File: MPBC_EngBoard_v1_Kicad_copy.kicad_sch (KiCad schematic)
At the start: 4 parts, among them Q1 NMOS, Q2 NMOS, U2 MP1909

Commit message: Gate Driver Circuit Progress (commit test)
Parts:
- added C1: 4.7uF, symbol Device:C
- added C2: 1uF, symbol Device:C
- added C3: 10uF, symbol Device:C
- added D1, D2, D3: MBR053T1G, symbol Device:D_Schottky
- added R2: 1.6Ω, symbol Device:R_US
- added R3: 4.7Ω, symbol Device:R_US
- R1: value R_US -> 1.6Ω
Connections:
- net at Q1.2 (G): now also R1.1, D1.2 (A)
- net at Q1.3 (S), Q2.1 (D): now also U2.6 (SW), C1.2
- net at R1.2: now also U2.5 (DRVH), D1.1 (K)
- net at Q2.2 (G): now also D2.2 (A), R2.1
- net at U2.1 (BST): now also D3.1 (K), R3.2
- net VCC: now reaches U2.4 (VCC)
- net VCC: now also C2.1, C3.1, D3.2 (A)
- net GND: now reaches U2.7 (GND)
- net GND: now also C2.2, C3.2
- net at U2.8 (DRVL): now also D2.1 (K), R2.2
- new net: C1.1, R3.1
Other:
- title: (none) -> Buck Converter Channel
- moved on the sheet: Q1, R1, U2

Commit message: Started LDO
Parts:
- added C4, C6, C7: 10uF, symbol Device:C
- added C5: 1uF, symbol Device:C
- added R4: 133Ω, symbol Device:R_US
- added R5: 400Ω, symbol Device:R_US
- added U1: LM1084-ADJ, symbol Regulator_Linear:LM1084-ADJ
- Q1, Q2: value NMOS -> BSZ018N04LS6
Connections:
- net GND: now also Q2.3 (S), C6.2, C7.2, R5.2
- net VCC renamed VREG
- net VREG: now also C6.1, C7.1, R4.1, U1.2 (VO)
- new net: R4.2, R5.1, U1.1 (ADJ)

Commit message: Buck Converter Circuit Finished
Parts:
- added C10, C9: 2.2nF, symbol Device:C
- added C11, C12, C13: 100uF, symbol Device:C_Polarized_US
- added C14, C15, C16, C17, C18, C19, C20, C21: 22uF, symbol Device:C
- added C8: 22nF, 0603, symbol Device:C
- added L1: 7.6uH, symbol Device:L
- added R10: 500uΩ, symbol Device:R_US
- added R6, R7: 0Ω, symbol Device:R_US
- added R8, R9: 750mΩ, symbol Device:R_US
- R4: value 133Ω -> 130Ω
- R5: value 400Ω -> 910Ω
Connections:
- net GND: now also C4.2, C5.2, C10.2, C11.2, C12.2, C13.2, C14.2, C15.2, C16.2, C17.2, C18.2, C19.2, C20.2, C21.2, C8.2, R6.2, R7.2; no longer C6.2, C7.2
- net BUCK_SW: now reaches C1.2, Q1.3 (S), Q2.1 (D), U2.6 (SW)
- net BUCK_SW: now also C9.2, L1.1, R9.1
- net VCC: now reaches C5.1
- net VCC: now also C4.1, U1.3 (VI)
- net VDD: now reaches Q1.1 (D)
- net VDD: now also R8.1
- net H_GATE: now reaches D1.2 (A), Q1.2 (G), R1.1
- net LDO_FB: now reaches R4.2, R5.1, U1.1 (ADJ)
- net LDO_FB: now also C8.1
- net GD_DRVH: now reaches D1.1 (K), R1.2, U2.5 (DRVH)
- net GD_DRVL: now reaches D2.1 (K), R2.2, U2.8 (DRVL)
- net L_GATE: now reaches D2.2 (A), Q2.2 (G), R2.1
- net GD_BST: now reaches D3.1 (K), R3.2, U2.1 (BST)
- new net: C9.1, R8.2
- new net: C10.1, R9.2
- new net: C6.2, R6.1
- new net: C7.2, R7.1
- new net BUCK_OUT: C11.1, C12.1, C13.1, C14.1, C15.1, C16.1, C17.1, C18.1, C19.1, C20.1, C21.1, L1.2, R10.1
- new net V_OUT: R10.2
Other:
- moved on the sheet: C1, C2, C3, C4, C5, C6, C7, D1, D2, D3, Q1, Q2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

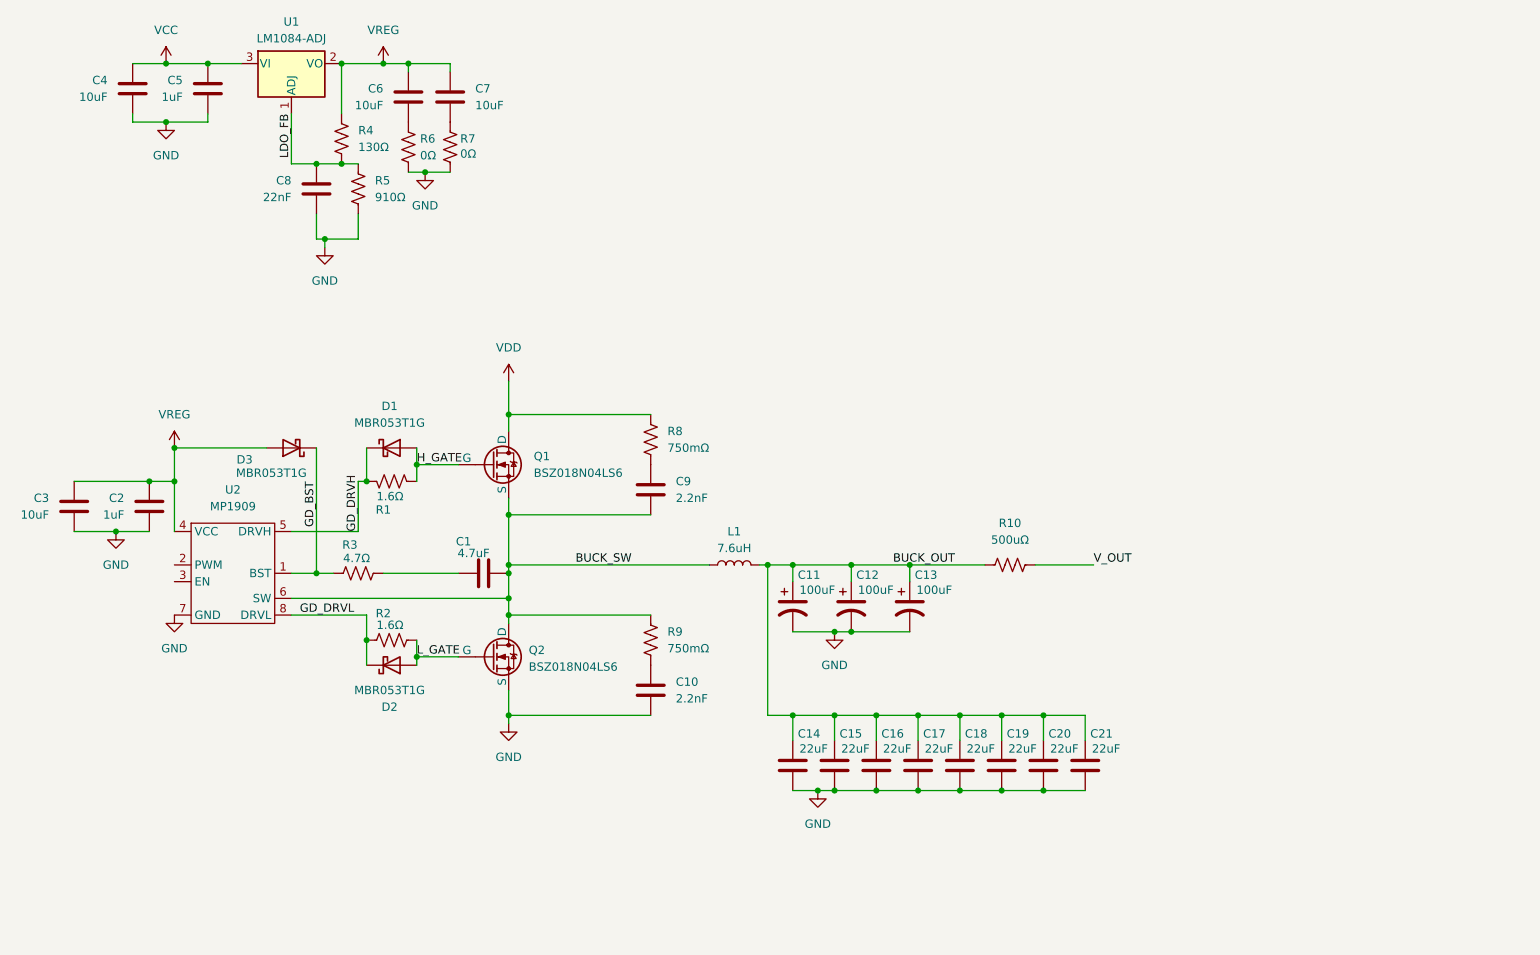
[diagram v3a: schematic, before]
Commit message: Updated to TPS7A24 regulator
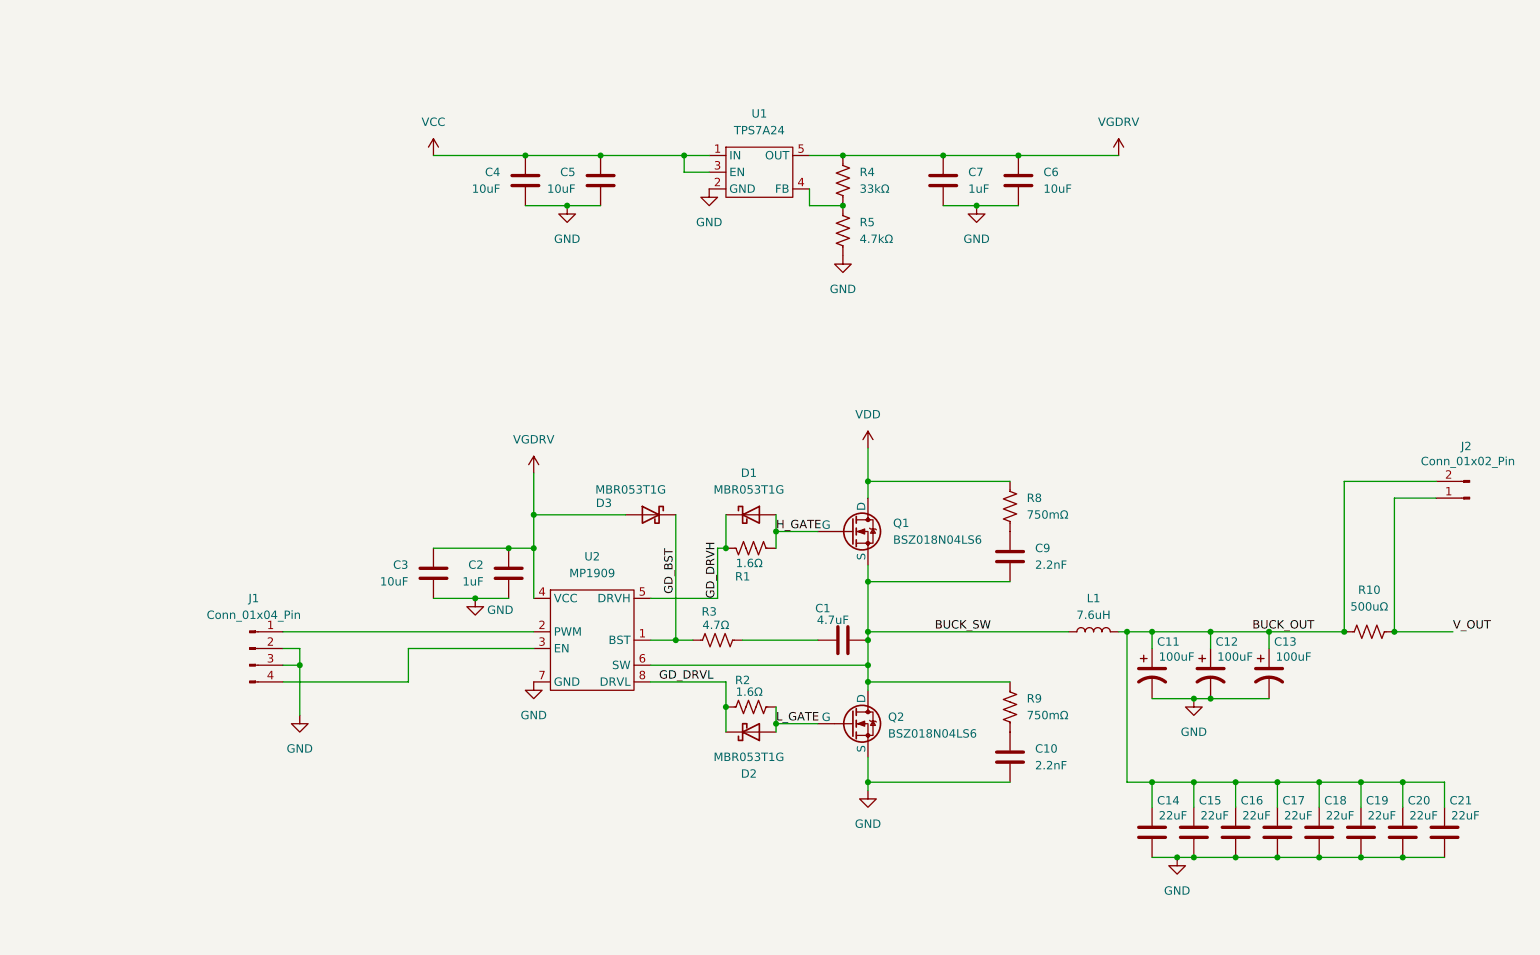
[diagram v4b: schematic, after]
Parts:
- removed C8: 22nF, 0603, symbol Device:C
- removed R6, R7: 0Ω, symbol Device:R_US
- removed U1: LM1084-ADJ, symbol Regulator_Linear:LM1084-ADJ
- added J1: Conn_01x04_Pin, symbol Connector:Conn_01x04_Pin
- added J2: Conn_01x02_Pin, symbol Connector:Conn_01x02_Pin
- added U1: TPS7A24, symbol MPBC_SchLib:TPS7A24
- C5: value 1uF -> 10uF
- C7: value 10uF -> 1uF
- R4: value 130Ω -> 33kΩ
- R5: value 910Ω -> 4.7kΩ
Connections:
- net BUCK_OUT: now also J2.2 (Pin_2)
- net GND: now also C6.2, C7.2, J1.2 (Pin_2), J1.3 (Pin_3), U1.2 (GND)
- net VCC: now also U1.1 (IN), U1.3 (EN)
- net V_OUT: now also J2.1 (Pin_1)
- net at U2.2 (PWM): now also J1.1 (Pin_1)
- net at U2.3 (EN): now also J1.4 (Pin_4)
- net LDO_FB: no longer names the net of R4.2, R5.1
- net LDO_FB: now also U1.4 (FB)
- net VREG renamed VGDRV
- net VGDRV: now also U1.5 (OUT)
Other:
- title: Buck Converter Channel -> Buck Converter Single Phase
- moved on the sheet: C1, C10, C11, C12, C13, C14, C15, C16, C17, C18, C19, C2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

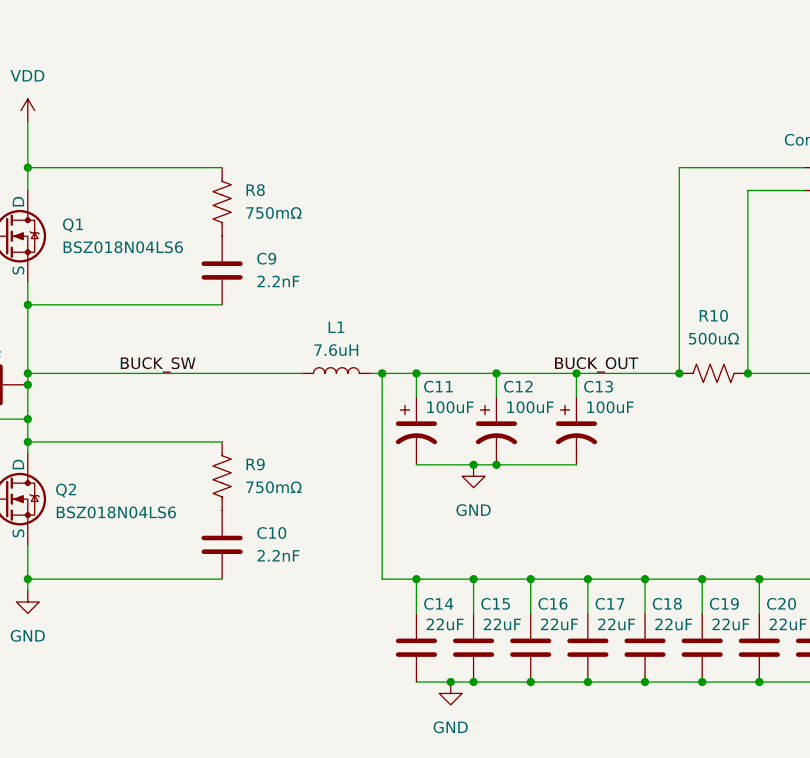
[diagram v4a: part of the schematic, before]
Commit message: DNP for snubber and most output caps
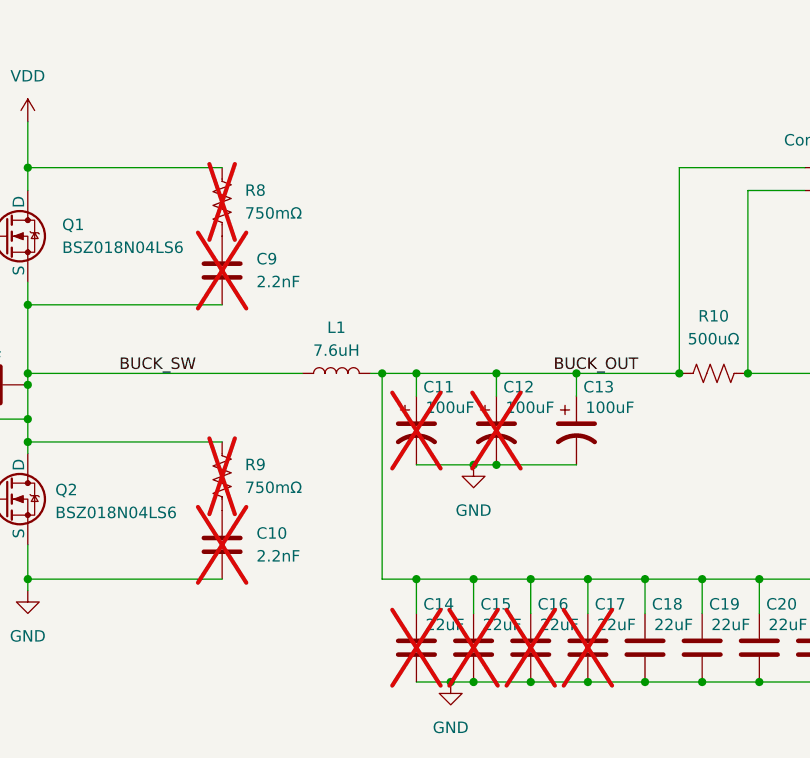
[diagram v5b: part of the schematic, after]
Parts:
- C10, C11, C12, C14, C15, C16, C17, C9, R8, R9: now not fitted
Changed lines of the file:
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@@
 		(in_bom yes)
 		(on_board yes)
-		(dnp no)
+		(dnp yes)
 		(fields_autoplaced yes)
 		(property "Reference" "R8"
@@
 		(in_bom yes)
 		(on_board yes)
-		(dnp no)
+		(dnp yes)
 		(property "Reference" "C9"
 			(at 166.37 97.7899 0)
@@
 		(in_bom yes)
 		(on_board yes)
-		(dnp no)
+		(dnp yes)
 		(property "Reference" "C12"
 			(at 193.802 112.014 0)
@@
 		(in_bom yes)
 		(on_board yes)
-		(dnp no)
+		(dnp yes)
 		(property "Reference" "C14"
 			(at 184.912 136.144 0)
@@
 		(in_bom yes)
 		(on_board yes)
-		(dnp no)
+		(dnp yes)
 		(property "Reference" "C11"
 			(at 184.912 112.014 0)
@@
 		(in_bom yes)
 		(on_board yes)
-		(dnp no)
+		(dnp yes)
 		(fields_autoplaced yes)
 		(property "Reference" "R9"
@@
 		(in_bom yes)
 		(on_board yes)
-		(dnp no)
+		(dnp yes)
 		(property "Reference" "C16"
 			(at 197.612 136.144 0)
@@
 		(in_bom yes)
 		(on_board yes)
-		(dnp no)
+		(dnp yes)
 		(property "Reference" "C15"
 			(at 191.262 136.144 0)
@@
 		(in_bom yes)
 		(on_board yes)
-		(dnp no)
+		(dnp yes)
 		(property "Reference" "C10"
 			(at 166.37 128.2699 0)
@@
 		(in_bom yes)
 		(on_board yes)
-		(dnp no)
+		(dnp yes)
 		(property "Reference" "C17"
 			(at 203.962 136.144 0)

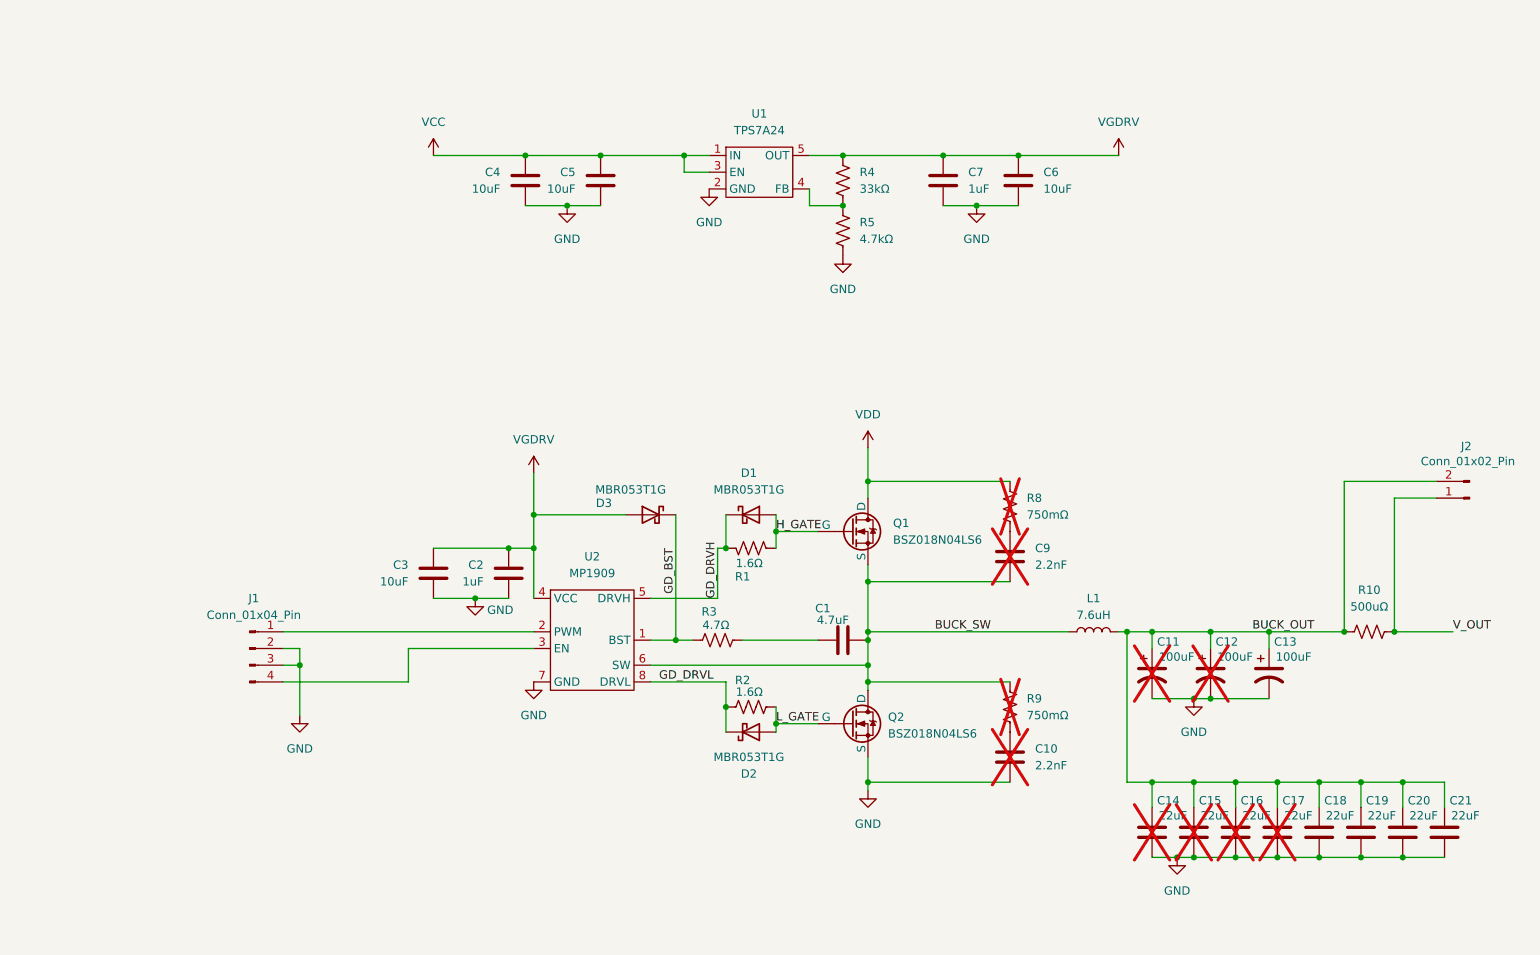
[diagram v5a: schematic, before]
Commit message: Updated labels to correspond to EasyEDA
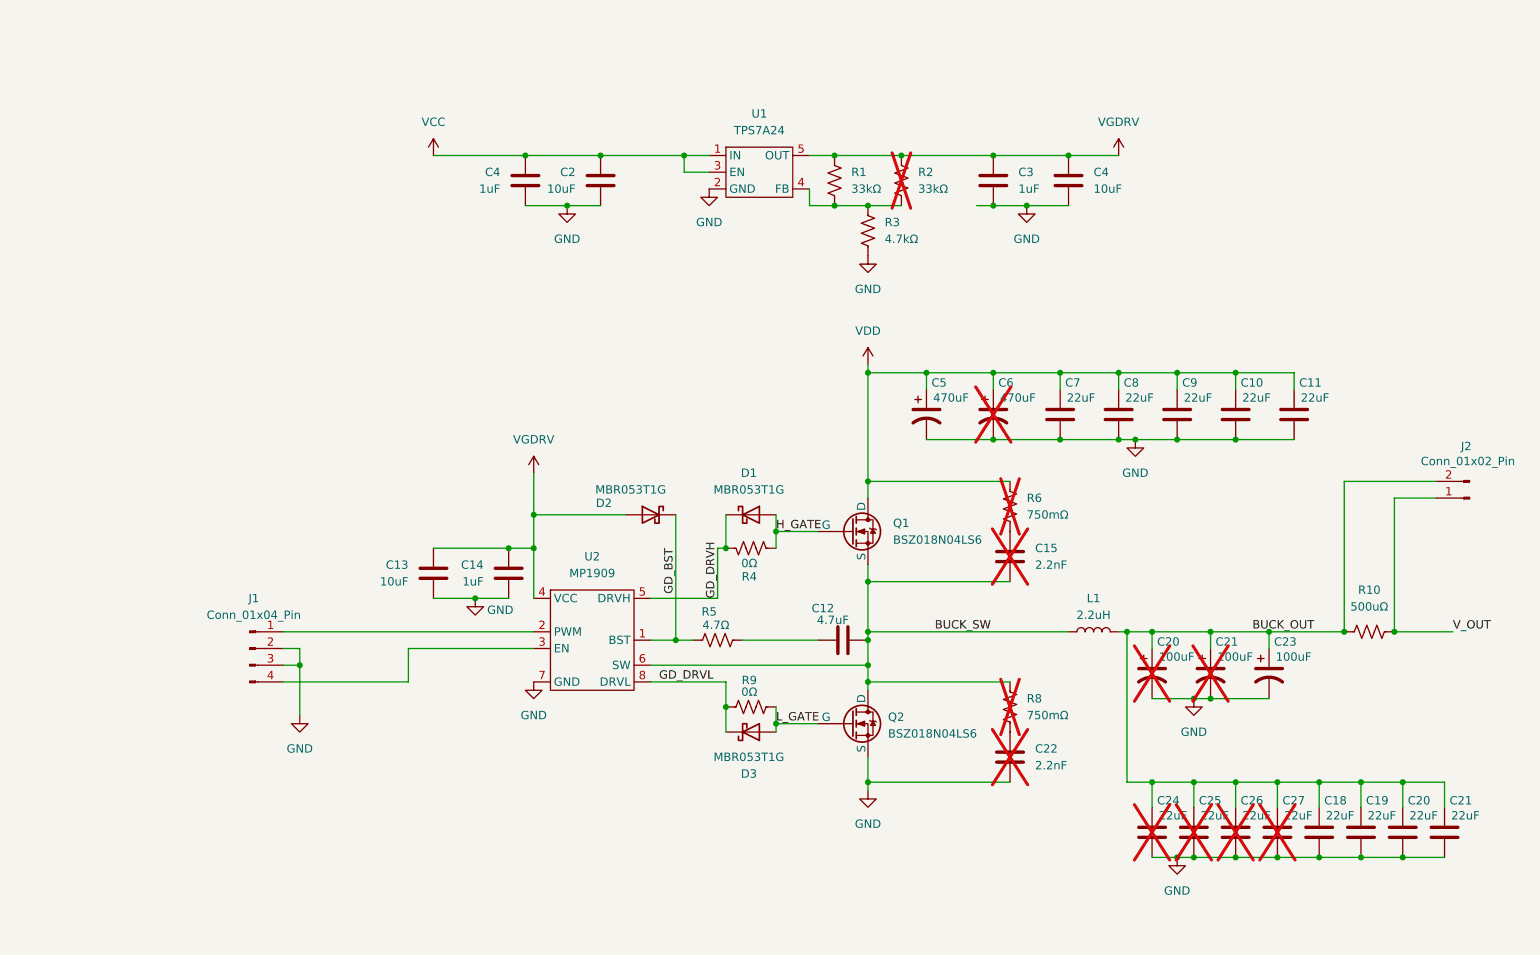
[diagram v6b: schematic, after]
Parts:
- added C10, C11, C7, C8, C9: 22uF, symbol Device:C
- added C5, C6: 470uF, symbol Device:C_Polarized_US
- added R2: 33kΩ, symbol Device:R_US
- C4: value 10uF -> 1uF
- L1: value 7.6uH -> 2.2uH
- R4: renamed from R1; value 1.6Ω -> 0Ω
- R9: renamed from R2; value 1.6Ω -> 0Ω
- renumbered C1 to C12, C3 to C13, C2 to C14, C9 to C15, C5 to C2, C11 to C20, C12 to C21, C10 to C22, C13 to C23, C14 to C24, C15 to C25, C16 to C26, C17 to C27, C7 to C3, C6 to C4, D3 to D2, D2 to D3, R4 to R1, R5 to R3, R3 to R5, R8 to R6, R9 to R8
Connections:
- net GND: now also C10.2, C11.2, C5.2, C6.2, C7.2, C8.2, C9.2
- net VDD: now also C10.1, C11.1, C5.1, C6.1, C7.1, C8.1, C9.1
- net VGDRV: now also R2.1
- net at R1.2, R3.1, U1.4 (FB): now also R2.2
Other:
- moved on the sheet: C3, C4, R1, R3
